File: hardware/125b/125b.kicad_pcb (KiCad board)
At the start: 2 copper layers, 59 x 75 mm, 49 parts, among them J1 Guitar in, J2 Barrel_Jack, J3 Conn_02x05_Odd_Even_MountingP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, J4 Guitar out, SW1 SW_Push_SPDT, SW2 RotaryEncoder_Switch, SW3 SW_Push, SW4 SW_Push, U1 L78L05_TO92, U2 TL074

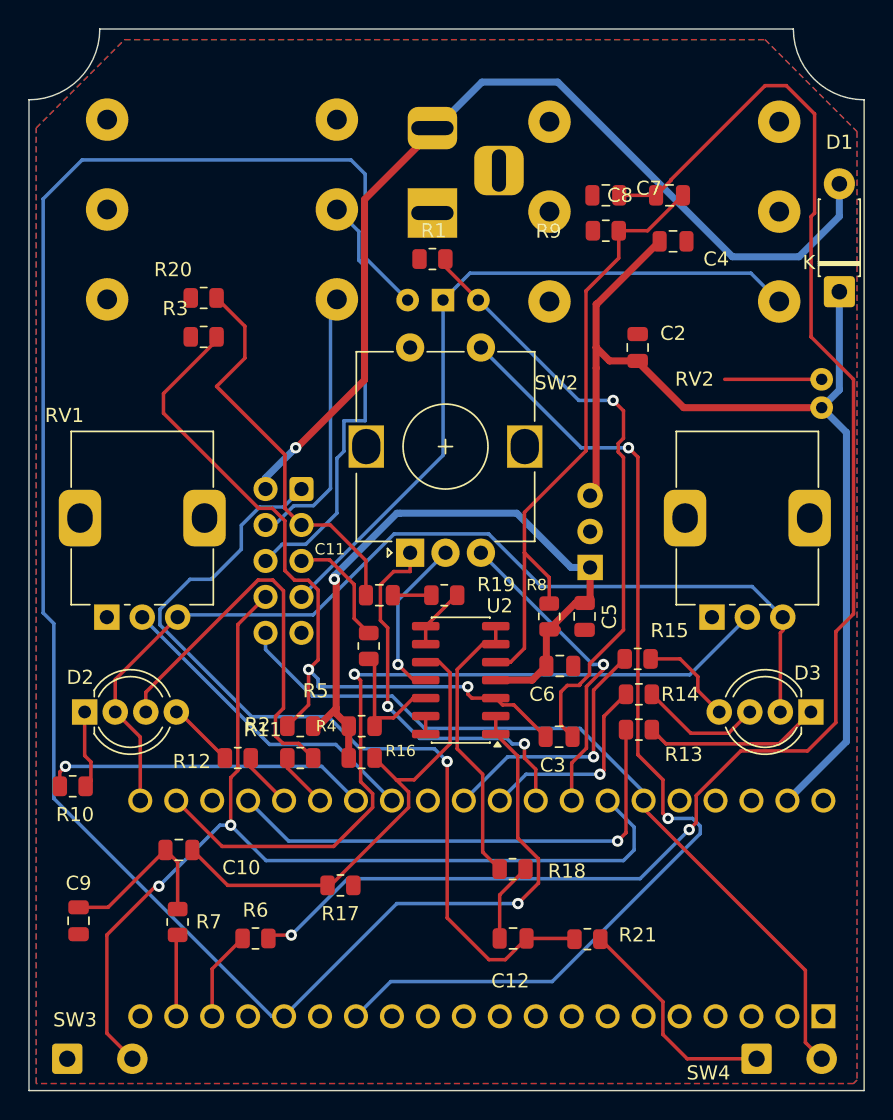
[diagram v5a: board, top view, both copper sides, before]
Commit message: Remove line in switch - TL074 is fine
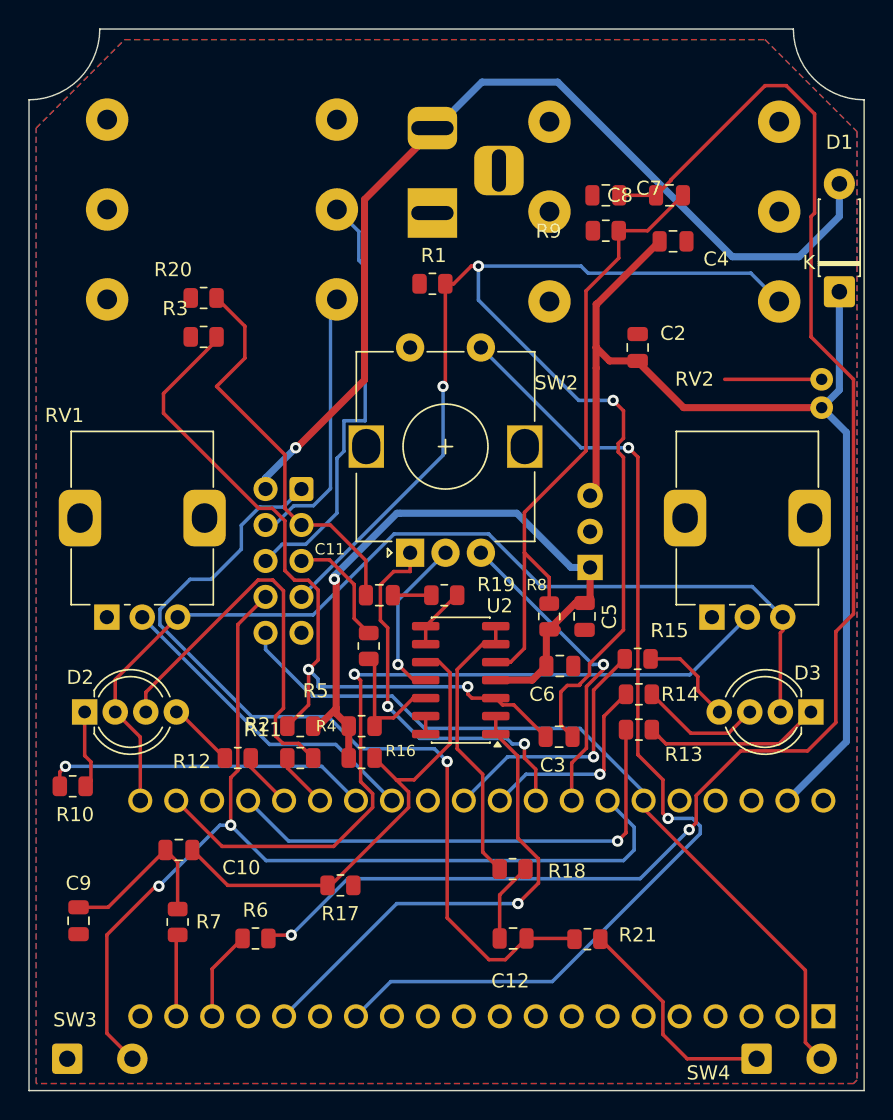
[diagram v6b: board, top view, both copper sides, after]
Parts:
- removed SW1: SW_Push_SPDT, Project:mini_switch_jaycar_SPDT
- moved R1 1.75 mm to (126.5, 53.0)
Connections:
- C3 pad 1: Net-(SW1-A) -> /fsw7
- R1 pad 1: Net-(SW1-A) -> /fsw7
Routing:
- net /Left in: track 134.7 -> 34.9 mm
- net Net-(SW1-A): track 43.4 -> 0.00 mm, vias 1 -> 0
- net /fsw7: track 50.7 -> 93.6 mm, vias 0 -> 3

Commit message: Tidy up labels on main pcb
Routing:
- net GND: track 42.8 -> 36.0 mm
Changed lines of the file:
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@@
 	(paper "A4")
 	(title_block
-		(date "2025-06-09")
-		(rev "0.4")
+		(date "2025-11-05")
+		(rev "0.7")
 	)
 	(layers
@@
 		)
 		(fp_text user "K"
-			(at 2.06 -2.15 0)
+			(at -2.44 -0.25 0)
 			(layer "F.SilkS")
 			(effects
@@
 		(tags "resistor")
 		(property "Reference" "R3"
-			(at 2 2 0)
+			(at 3.0875 0 0)
 			(layer "F.SilkS")
 			(effects
@@
 		(tags "resistor")
 		(property "Reference" "R4"
-			(at -2.5 0 0)
+			(at 2.5 0.75 0)
 			(layer "F.SilkS")
 			(effects
@@
 		(tags "Potentiometer vertical Alps RK09K RK09D Single Snapin")
 		(property "Reference" "RV2"
-			(at 16.813178 -1.236822 180)
+			(at 13.8 -4.25 180)
 			(layer "F.SilkS")
 			(effects
@@
 		(tags "resistor")
 		(property "Reference" "R2"
-			(at 3.019805 0.095577 0)
+			(at 5.6625 0 0)
 			(layer "F.SilkS")
 			(effects
@@
 		(tags "capacitor")
 		(property "Reference" "C7"
-			(at 3.05 -0.5 0)
+			(at -1.25 -2.25 0)
 			(layer "F.SilkS")
 			(effects
@@
 		(tags "resistor")
 		(property "Reference" "R9"
-			(at 4.048828 -0.031866 0)
+			(at 3 -1.25 0)
 			(layer "F.SilkS")
 			(effects
@@
 		(tags "resistor")
 		(property "Reference" "R13"
-			(at 3.1625 1.75 0)
+			(at 2.9125 2 0)
 			(layer "F.SilkS")
 			(effects
@@
 		(tags "resistor")
 		(property "Reference" "R11"
-			(at -2.6625 -2 0)
+			(at 0.3375 5 0)
 			(layer "F.SilkS")
 			(effects
@@
 		(tags "capacitor")
 		(property "Reference" "C4"
-			(at -3.05 -1.25 0)
+			(at -3.25 0 0)
 			(layer "F.SilkS")
 			(effects
@@
 		(tags "rotary encoder")
 		(property "Reference" "SW2"
-			(at 12 10.325 180)
+			(at 17 -1.175 180)
 			(layer "F.SilkS")
 			(effects
@@
 		(tags "capacitor")
 		(property "Reference" "C8"
-			(at -3.5 0 0)
+			(at 3.25 0 0)
 			(layer "F.SilkS")
 			(effects
@@
 		(tags "resistor")
 		(property "Reference" "R1"
-			(at -0.0875 2 180)
+			(at 3 0.75 180)
 			(layer "F.SilkS")
 			(effects
@@
 		(tags "connector wire 0.5sqmm")
 		(property "Reference" "SW3"
-			(at 0.55 -2.75 0)
+			(at 8.3 0.75 0)
 			(layer "F.SilkS")
 			(effects
@@
 		(tags "resistor")
 		(property "Reference" "R16"
-			(at 2.75 -0.5 0)
+			(at 3 -0.25 0)
 			(layer "F.SilkS")
 			(effects
@@
 		(tags "resistor")
 		(property "Reference" "R20"
-			(at 2.1625 2 0)
+			(at 3.3375 1.25 0)
 			(layer "F.SilkS")
 			(effects
@@
 		(tags "neutrik jack m")
 		(property "Reference" "J1"
-			(at 1.435 -18.792086 90)
+			(at -5.5 -1.5 180)
 			(layer "B.SilkS")
 			(effects
@@
 		(tags "neutrik jack m")
 		(property "Reference" "J4"
-			(at 6.35 3 90)
+			(at -6.15 -15.5 180)
 			(layer "B.SilkS")
 			(effects
@@
 		(tags "Through hole vertical IDC box header THT 2x05 2.54mm double row")
 		(property "Reference" "J3"
-			(at 1.25 -17 180)
+			(at -5.25 -8.5 180)
 			(layer "B.SilkS")
 			(effects
@@
 		(tags "Power Jack")
 		(property "Reference" "J2"
-			(at -8 -5.7075 90)
+			(at 2 -4.25 180)
 			(layer "B.SilkS")
 			(effects
@@
 		(width 0.25)
 		(layer "F.Cu")
-		(net 20)
-	)
-	(segment
-		(start 147.15 59.75)
-		(end 154 59.75)
-		(width 0.25)
-		(layer "F.Cu")
